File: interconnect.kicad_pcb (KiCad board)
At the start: 2 copper layers, 50 x 101.3 mm, 3 parts, among them J1 Conn_02x22_Top_Bottom, J2 Conn_02x22_Top_Bottom

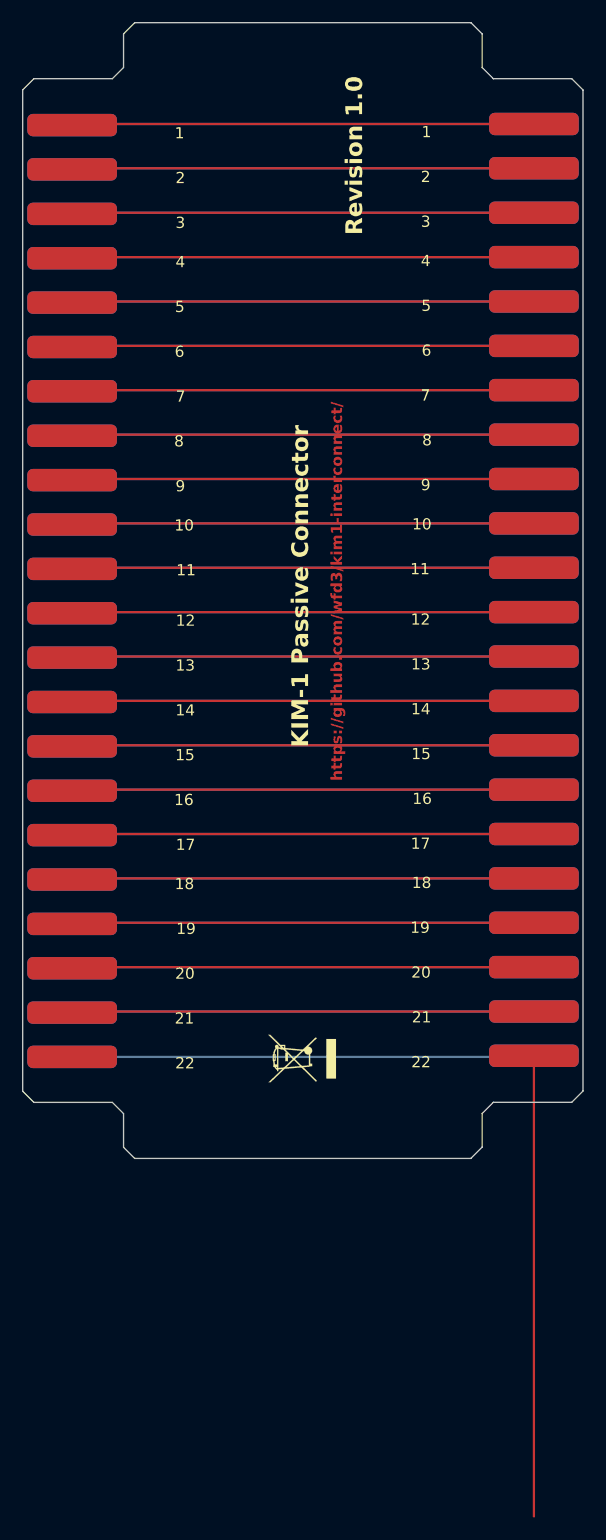
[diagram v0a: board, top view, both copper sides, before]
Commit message: Increase trace width to reduce resistance.
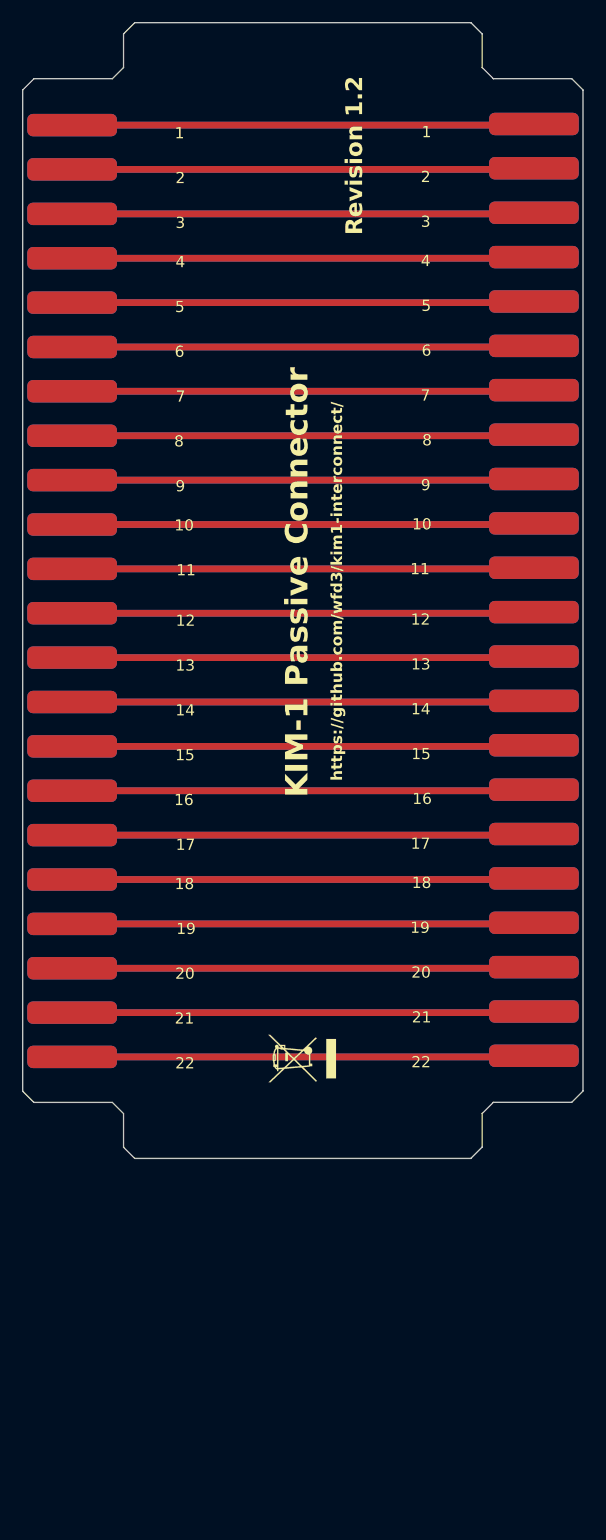
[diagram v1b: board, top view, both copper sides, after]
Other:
- board text added: "Revision 1.2"
- board text removed: "Revision 1.0"
